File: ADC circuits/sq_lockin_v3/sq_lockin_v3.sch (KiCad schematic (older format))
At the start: 29 parts, among them J1 battery, J10 Conn_01x03_Male, J11 Conn_01x02_Male_2.54mm, J2 Conn_01x02_Male_2.54mm, J21 Conn_01x02_Male_2.54mm, J3 DB9_Female_MountingHoles, J4 Conn_01x02_Male_2.54mm, J5 Conn_01x02_Male_2.54mm, J6 receptacle, J8 USB_C_KoreanHroparts_6P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

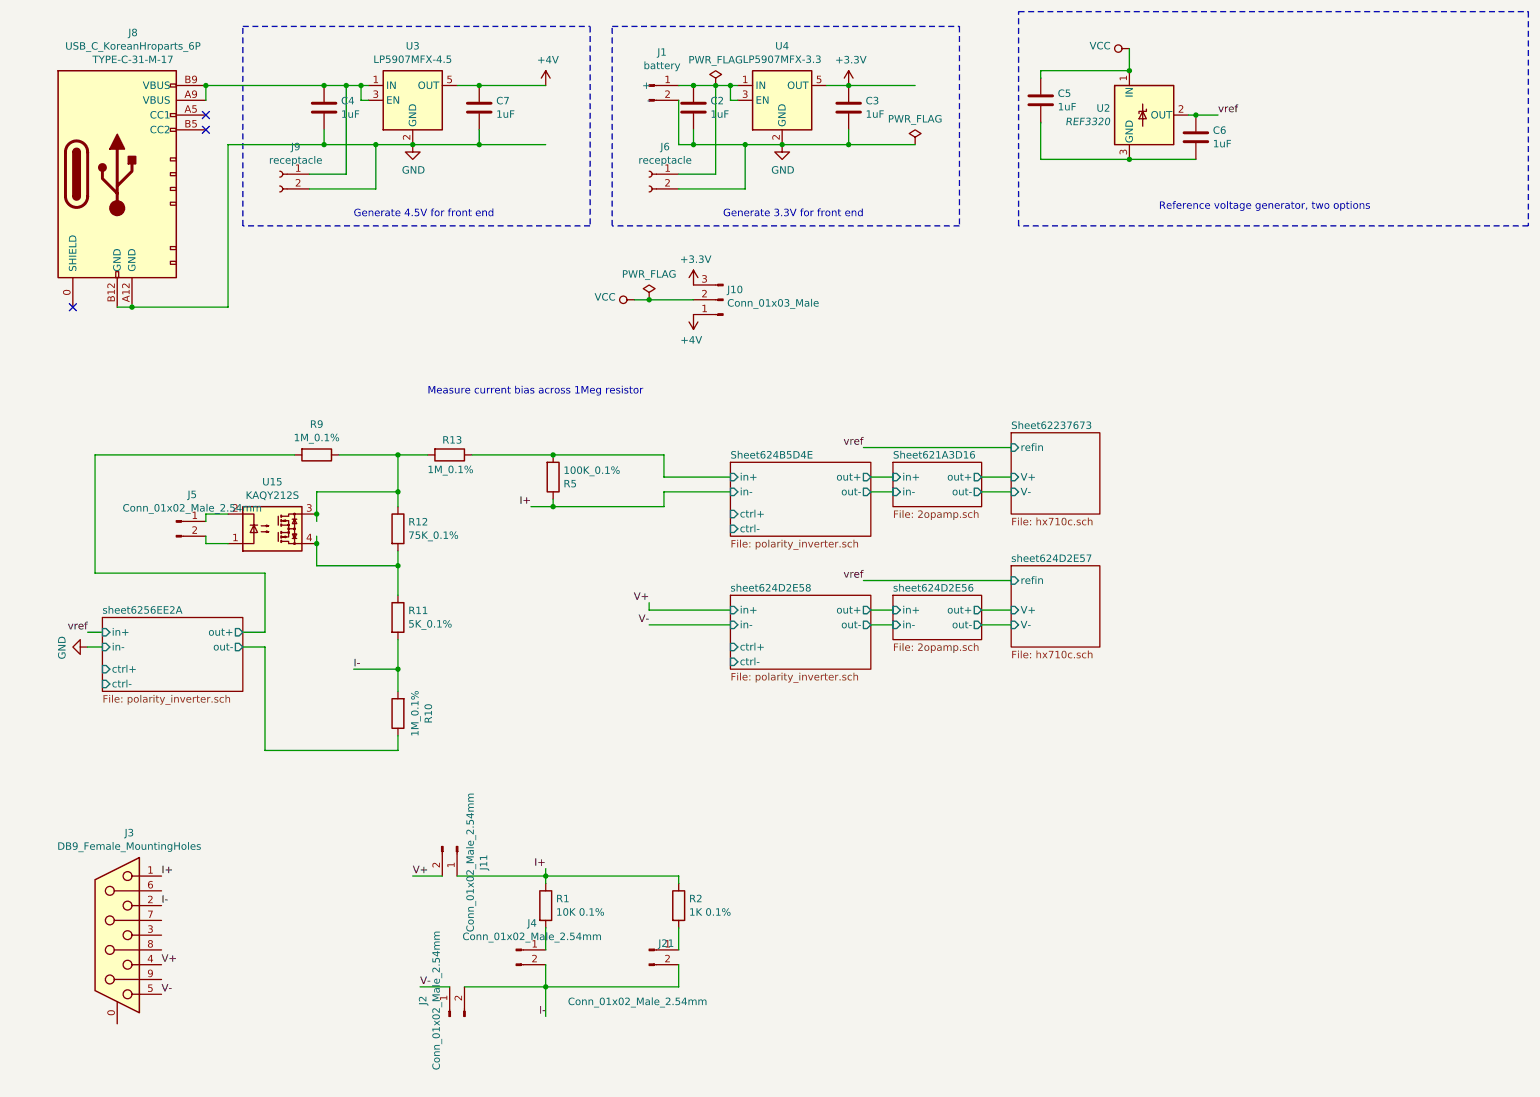
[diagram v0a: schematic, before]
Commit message: Add power-two-wre and tweaks to sq_lockin_v3
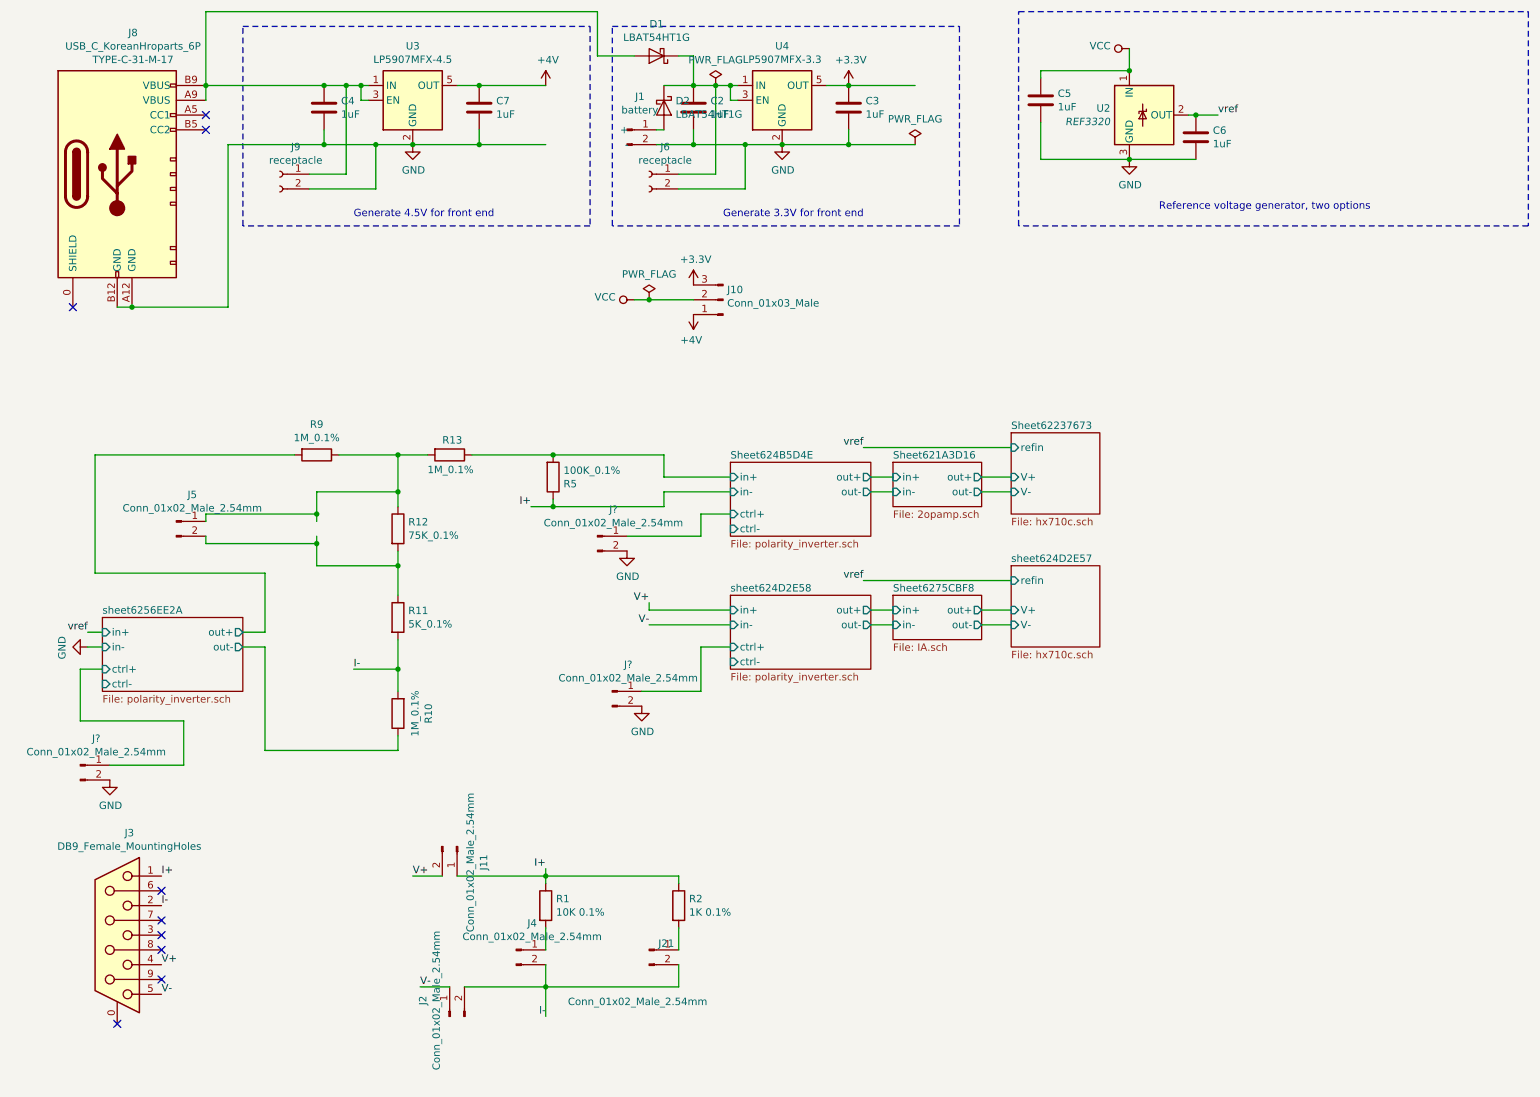
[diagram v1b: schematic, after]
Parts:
- removed U15: KAQY212S, 0my_footprints:SOP-4_L4.4-W4.0-P2.54-LS7.0-BL, symbol 0JLC:KAQY212S
- added D1, D2: LBAT54HT1G, Diode_SMD:D_SOD-323, symbol 0JLC:LBAT54HT1G
- added J? (x3): Conn_01x02_Male_2.54mm, Connector_PinHeader_2.54mm:PinHeader_1x02_P2.54mm_Vertical, symbol 0JLC:Conn_01x02_Male_2.54mm
- J11, J2, J21, J4, J5: LCSC C492401 -> C358684; MPN PZ254V-11-02P -> MTP125-1102S1
- J3: footprint Connector_Dsub:DSUB-9_Female_Horizontal_P2.77x2.84mm_EdgePinOffset4.94mm_Housed_MountingHolesOffset7.48mm -> 0my_footprints:DSUB-TH_DS1037-09FNAKT74-0CC; LCSC (none) -> C75749; MPN (none) -> DS1037-09FNAKT74-0CC
- U2: footprint Package_TO_SOT_SMD:SOT-23 -> Package_TO_SOT_SMD:SOT-323_SC-70; LCSC (none) -> C134146; MPN (none) -> REF3320AIDCKT
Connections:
- wire segments 119 -> 136
- no-connect marks 3 -> 9
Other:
- note removed: "Measure current bias across 1Meg resistor"
- moved on the sheet: J1

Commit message: add uart mux versions
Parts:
- added C10, C11: 1uF, Capacitor_SMD:C_0603_1608Metric_Pad1.05x0.95mm_HandSolder, symbol 0JLC:1uF
- added J16: Conn_01x03_Male, Connector_PinHeader_2.54mm:PinHeader_1x03_P2.54mm_Vertical, symbol Connector:Conn_01x03_Male
- added U9: REF3030, Package_TO_SOT_SMD:SOT-23, symbol Reference_Voltage:REF3030
- U2: value REF3320 -> REF3325; footprint Package_TO_SOT_SMD:SOT-323_SC-70 -> Package_TO_SOT_SMD:SOT-23; symbol Reference_Voltage:REF3020 -> Reference_Voltage:REF3033; LCSC C134146 -> C69039; MPN REF3320AIDCKT -> REF3325AIDBZR
- gave numbers to parts that had none: 3
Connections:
- net labels added: vref1, vref2
- wire segments 136 -> 143
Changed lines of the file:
@@
 Connection ~ 8300 1350
 Text Label 8450 1350 0    50   ~ 0
-vref
+vref1
 $Comp
 L power:VCC #PWR0101
@@
 NoConn ~ 1300 7200
 $Comp
-L Reference_Voltage:REF3020 U2
+L Reference_Voltage:REF3033 U2
 U 1 1 624F54A5
 P 7950 1350
 F 0 "U2" H 7721 1396 50  0000 R CNN
-F 1 "REF3320" H 7721 1305 50  0000 R CIN
-F 2 "Package_TO_SOT_SMD:SOT-323_SC-70" H 7950 900 50  0001 C CIN
+F 1 "REF3325" H 7721 1305 50  0000 R CIN
+F 2 "Package_TO_SOT_SMD:SOT-23" H 7950 900 50  0001 C CIN
 F 3 "http://www.ti.com/lit/ds/symlink/ref3033.pdf" H 8050 1000 50  0001 C CIN
-F 4 "C134146" H 7950 1350 50  0001 C CNN "LCSC"
-F 5 "REF3320AIDCKT" H 7950 1350 50  0001 C CNN "MPN"
+F 4 "C69039" H 7950 1350 50  0001 C CNN "LCSC"
+F 5 "REF3325AIDBZR" H 7950 1350 50  0001 C CNN "MPN"
 	1    7950 1350
 	1    0    0    -1
 $EndComp
 $Comp
-L 0JLC:Conn_01x02_Male_2.54mm J?
+L 0JLC:Conn_01x02_Male_2.54mm J12
 U 1 1 6290AEA9
 P 750 5750
-F 0 "J?" H 858 5931 50  0000 C CNN
+F 0 "J12" H 858 5931 50  0000 C CNN
 F 1 "Conn_01x02_Male_2.54mm" H 858 5840 50  0000 C CNN
 F 2 "Connector_PinHeader_2.54mm:PinHeader_1x02_P2.54mm_Vertical" H 750 5750 50  0001 C CNN
@@
 $EndComp
 $Comp
-L power:GND #PWR?
+L power:GND #PWR0103
 U 1 1 6290CA07
 P 950 5850
-F 0 "#PWR?" H 950 5600 50  0001 C CNN
+F 0 "#PWR0103" H 950 5600 50  0001 C CNN
 F 1 "GND" H 955 5677 50  0000 C CNN
 F 2 "" H 950 5850 50  0001 C CNN
@@
 $EndComp
 $Comp
-L 0JLC:Conn_01x02_Male_2.54mm J?
+L 0JLC:Conn_01x02_Male_2.54mm J15
 U 1 1 6290D581
 P 4350 5250
-F 0 "J?" H 4458 5431 50  0000 C CNN
+F 0 "J15" H 4458 5431 50  0000 C CNN
 F 1 "Conn_01x02_Male_2.54mm" H 4458 5340 50  0000 C CNN
 F 2 "Connector_PinHeader_2.54mm:PinHeader_1x02_P2.54mm_Vertical" H 4350 5250 50  0001 C CNN
@@
 $EndComp
 $Comp
-L power:GND #PWR?
+L power:GND #PWR0104
 U 1 1 6290D587
 P 4550 5350
-F 0 "#PWR?" H 4550 5100 50  0001 C CNN
+F 0 "#PWR0104" H 4550 5100 50  0001 C CNN
 F 1 "GND" H 4555 5177 50  0000 C CNN
 F 2 "" H 4550 5350 50  0001 C CNN
@@
 $EndComp
 $Comp
-L 0JLC:Conn_01x02_Male_2.54mm J?
+L 0JLC:Conn_01x02_Male_2.54mm J14
 U 1 1 62913148
 P 4250 4200
-F 0 "J?" H 4358 4381 50  0000 C CNN
+F 0 "J14" H 4358 4381 50  0000 C CNN
 F 1 "Conn_01x02_Male_2.54mm" H 4358 4290 50  0000 C CNN
 F 2 "Connector_PinHeader_2.54mm:PinHeader_1x02_P2.54mm_Vertical" H 4250 4200 50  0001 C CNN
@@
 $EndComp
 $Comp
-L power:GND #PWR?
+L power:GND #PWR0107
 U 1 1 6291314E
 P 4450 4300
-F 0 "#PWR?" H 4450 4050 50  0001 C CNN
+F 0 "#PWR0107" H 4450 4050 50  0001 C CNN
 F 1 "GND" H 4455 4127 50  0000 C CNN
 F 2 "" H 4450 4300 50  0001 C CNN
@@
 Wire Wire Line
 	750  5100 900  5100
+$Comp
+L Reference_Voltage:REF3030 U9
+U 1 1 629878A0
+P 9750 1350
+F 0 "U9" H 9521 1396 50  0000 R CNN
+F 1 "REF3030" H 9521 1305 50  0000 R CIN
+F 2 "Package_TO_SOT_SMD:SOT-23" H 9750 900 50  0001 C CIN
+F 3 "http://www.ti.com/lit/ds/symlink/ref3033.pdf" H 9850 1000 50  0001 C CIN
+F 4 "C38423" H 9750 1350 50  0001 C CNN "LCSC"
+F 5 "REF3030AIDBZR" H 9750 1350 50  0001 C CNN "MPN"
+	1    9750 1350
+	1    0    0    -1
+$EndComp
+$Comp
+L 0JLC:1uF C11
+U 1 1 6298972C
+P 10200 1500
+F 0 "C11" H 10315 1546 50  0000 L CNN
+F 1 "1uF" H 10315 1455 50  0000 L CNN
+F 2 "Capacitor_SMD:C_0603_1608Metric_Pad1.05x0.95mm_HandSolder" H 10238 1350 50  0001 C CNN
+F 3 "~" H 10200 1500 50  0001 C CNN
+F 4 "C15849" H 10200 1500 50  0001 C CNN "LCSC"
+F 5 "CL10A105KB8NNNC" H 10200 1500 50  0001 C CNN "MPN"
+	1    10200 1500
+	1    0    0    -1
+$EndComp
+$Comp
+L 0JLC:1uF C10
+U 1 1 62989F81
+P 9050 1150
+F 0 "C10" H 9165 1196 50  0000 L CNN
+F 1 "1uF" H 9165 1105 50  0000 L CNN
+F 2 "Capacitor_SMD:C_0603_1608Metric_Pad1.05x0.95mm_HandSolder" H 9088 1000 50  0001 C CNN
+F 3 "~" H 9050 1150 50  0001 C CNN
+F 4 "C15849" H 9050 1150 50  0001 C CNN "LCSC"
+F 5 "CL10A105KB8NNNC" H 9050 1150 50  0001 C CNN "MPN"
+	1    9050 1150
+	1    0    0    -1
+$EndComp
+Wire Wire Line
+	9050 1000 9300 1000
+Wire Wire Line
+	9650 1000 9650 1050
+Wire Wire Line
+	10200 1350 10050 1350
+Wire Wire Line
+	10200 1650 9650 1650
+Wire Wire Line
+	9050 1650 9050 1300
+Connection ~ 9650 1650
+Wire Wire Line
+	9650 1650 9050 1650
+$Comp
+L power:GND #PWR0109
+U 1 1 6299CD8C
+P 9650 1650
+F 0 "#PWR0109" H 9650 1400 50  0001 C CNN
+F 1 "GND" H 9655 1477 50  0000 C CNN
+F 2 "" H 9650 1650 50  0001 C CNN
+F 3 "" H 9650 1650 50  0001 C CNN
+	1    9650 1650
+	1    0    0    -1
+$EndComp
+$Comp
+L power:VCC #PWR0111
+U 1 1 6299D337
+P 9300 1000
+F 0 "#PWR0111" H 9300 850 50  0001 C CNN
+F 1 "VCC" V 9318 1127 50  0000 L CNN
+F 2 "" H 9300 1000 50  0001 C CNN
+F 3 "" H 9300 1000 50  0001 C CNN
+	1    9300 1000
+	1    0    0    -1
+$EndComp
+Connection ~ 9300 1000
+Wire Wire Line
+	9300 1000 9650 1000
+Text Label 10200 1350 0    50   ~ 0
+vref2
+$Comp
+L Connector:Conn_01x03_Male J16
+U 1 1 629A62B2
+P 8900 2450
+F 0 "J16" H 8872 2382 50  0000 R CNN
+F 1 "Conn_01x03_Male" H 8872 2473 50  0000 R CNN
+F 2 "Connector_PinHeader_2.54mm:PinHeader_1x03_P2.54mm_Vertical" H 8900 2450 50  0001 C CNN
+F 3 "~" H 8900 2450 50  0001 C CNN
+F 4 "C49257" H 8900 2450 50  0001 C CNN "LCSC"
+F 5 "" H 8900 2450 50  0001 C CNN "MPN"
+	1    8900 2450
+	-1   0    0    1
+$EndComp
+Text Label 8700 2350 2    50   ~ 0
+vref1
+Text Label 8700 2550 2    50   ~ 0
+vref2
+Text Label 8700 2450 2    50   ~ 0
+vref
 $EndSCHEMATC
